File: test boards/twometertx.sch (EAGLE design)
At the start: 12 parts

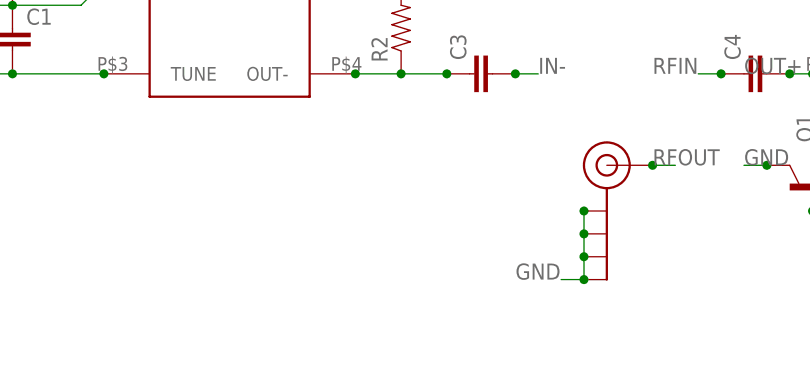
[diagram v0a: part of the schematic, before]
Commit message: 2 meter rx fixes
added ground pours and 4 pin header to the 2 meter rx for a test board.
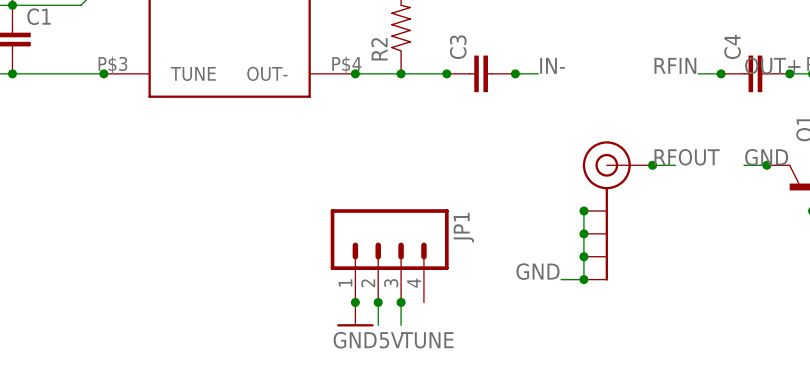
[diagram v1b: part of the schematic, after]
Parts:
- added JP1: (no value), SparkFun-Connectors:M04LONGPADS
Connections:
- net 5V: now also JP1.2
- net GND: now also JP1.1
- net TUNE: now also JP1.3
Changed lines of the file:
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@@
 <?xml version="1.0" encoding="utf-8"?>
 <!DOCTYPE eagle SYSTEM "eagle.dtd">
-<eagle version="7.2.0">
+<eagle version="7.3.0">
 <drawing>
 <settings>
@@
 <layer number="56" name="wert" color="7" fill="1" visible="no" active="no"/>
 <layer number="57" name="tCAD" color="7" fill="1" visible="no" active="no"/>
+<layer number="59" name="tCarbon" color="7" fill="1" visible="no" active="no"/>
+<layer number="60" name="bCarbon" color="7" fill="1" visible="no" active="no"/>
 <layer number="90" name="Modules" color="5" fill="1" visible="yes" active="yes"/>
 <layer number="91" name="Nets" color="2" fill="1" visible="yes" active="yes"/>
@@
 <layer number="113" name="IDFDebug" color="4" fill="1" visible="yes" active="yes"/>
 <layer number="116" name="Patch_BOT" color="9" fill="4" visible="yes" active="yes"/>
+<layer number="118" name="Rect_Pads" color="7" fill="1" visible="yes" active="yes"/>
 <layer number="121" name="_tsilk" color="7" fill="1" visible="yes" active="yes"/>
 <layer number="122" name="_bsilk" color="7" fill="1" visible="yes" active="yes"/>
@@
 <layer number="127" name="_tValues" color="7" fill="1" visible="yes" active="yes"/>
 <layer number="128" name="_bValues" color="7" fill="1" visible="yes" active="yes"/>
+<layer number="129" name="Mask" color="7" fill="1" visible="yes" active="yes"/>
 <layer number="131" name="tAdjust" color="7" fill="1" visible="yes" active="yes"/>
 <layer number="132" name="bAdjust" color="7" fill="1" visible="yes" active="yes"/>
@@
 <layer number="223" name="223bmp" color="24" fill="1" visible="no" active="no"/>
 <layer number="224" name="224bmp" color="25" fill="1" visible="no" active="no"/>
+<layer number="225" name="225bmp" color="7" fill="1" visible="yes" active="yes"/>
+<layer number="226" name="226bmp" color="7" fill="1" visible="yes" active="yes"/>
+<layer number="227" name="227bmp" color="7" fill="1" visible="yes" active="yes"/>
+<layer number="228" name="228bmp" color="7" fill="1" visible="yes" active="yes"/>
+<layer number="229" name="229bmp" color="7" fill="1" visible="yes" active="yes"/>
+<layer number="230" name="230bmp" color="7" fill="1" visible="yes" active="yes"/>
+<layer number="231" name="231bmp" color="7" fill="1" visible="yes" active="yes"/>
 <layer number="248" name="Housing" color="7" fill="1" visible="yes" active="yes"/>
 <layer number="249" name="Edge" color="7" fill="1" visible="yes" active="yes"/>
@@
 <layer number="251" name="SMDround" color="12" fill="11" visible="no" active="no"/>
 <layer number="254" name="cooling" color="7" fill="1" visible="yes" active="yes"/>
+<layer number="255" name="routoute" color="7" fill="1" visible="yes" active="yes"/>
 </layers>
 <schematic xreflabel="%F%N/%S.%C%R" xrefpart="/%S.%C%R">
@@
 <part name="J$1" library="SparkFun-Connectors" deviceset="SMA_EDGE" device=""/>
 <part name="Q1" library="SparkFun-DiscreteSemi" deviceset="TRANSISTOR_NPN" device="SOT89"/>
+<part name="JP1" library="SparkFun-Connectors" deviceset="M04" device="LONGPADS"/>
+<part name="GND2" library="SparkFun-Aesthetics" deviceset="GND" device=""/>
 </parts>
 <sheets>
@@
 <instance part="J$1" gate="1" x="86.36" y="30.48"/>
 <instance part="Q1" gate="G$1" x="109.22" y="27.94" rot="R90"/>
+<instance part="JP1" gate="G$1" x="60.96" y="20.32" rot="R270"/>
+<instance part="GND2" gate="1" x="58.42" y="12.7"/>
 </instances>
 <busses>
@@
 <label x="76.2" y="17.78" size="1.778" layer="95"/>
 </segment>
+<segment>
+<pinref part="JP1" gate="G$1" pin="1"/>
+<pinref part="GND2" gate="1" pin="GND"/>
+<junction x="58.42" y="15.24"/>
+</segment>
 </net>
 <net name="TUNE" class="0">
@@
 <junction x="30.48" y="40.64"/>
 <label x="10.16" y="40.64" size="1.778" layer="95"/>
+</segment>
+<segment>
+<wire x1="63.5" y1="15.24" x2="63.5" y2="12.7" width="0.1524" layer="91"/>
+<label x="63.5" y="10.16" size="1.778" layer="95"/>
+<pinref part="JP1" gate="G$1" pin="3"/>
+<junction x="63.5" y="15.24"/>
 </segment>
 </net>
@@
 <junction x="139.7" y="60.96"/>
 </segment>
-</net>
+<segment>
+<wire x1="60.96" y1="12.7" x2="60.96" y2="15.24" width="0.1524" layer="91"/>
+<label x="60.96" y="10.16" size="1.778" layer="95"/>
+<pinref part="JP1" gate="G$1" pin="2"/>
+<junction x="60.96" y="15.24"/>
+</segment>
+</net>

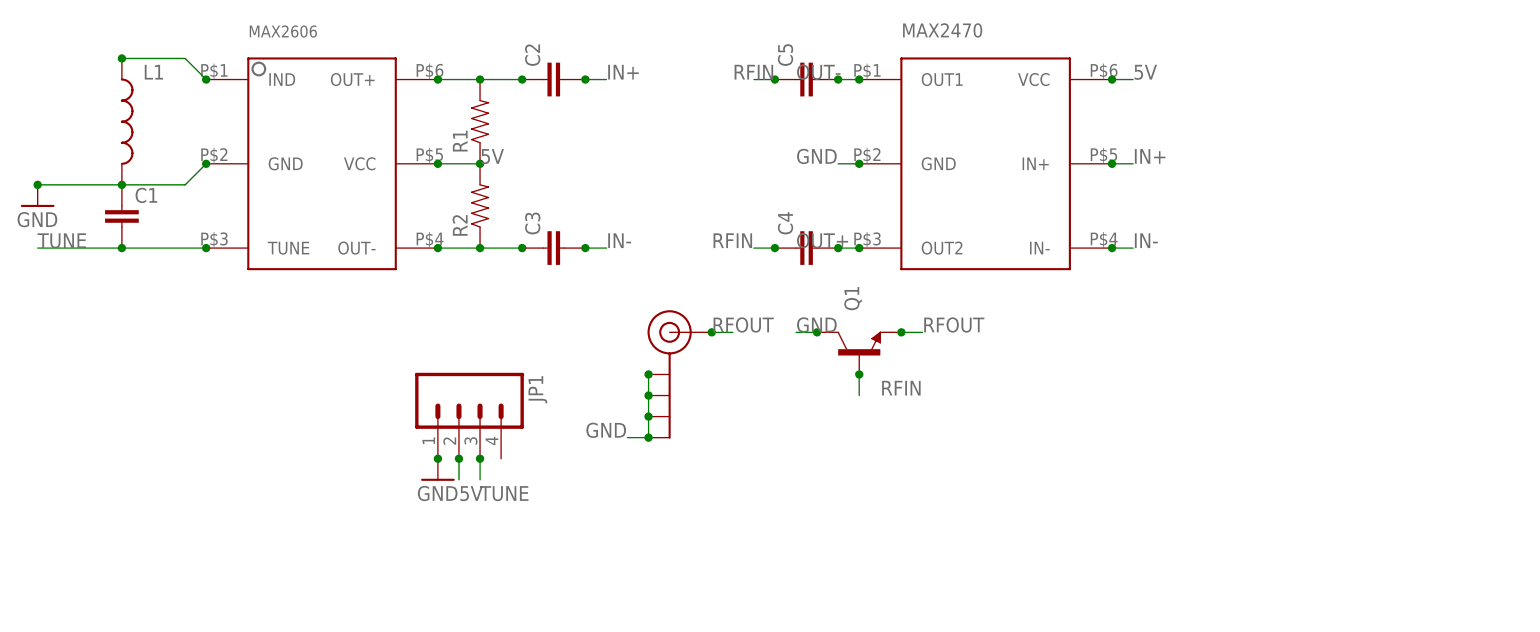
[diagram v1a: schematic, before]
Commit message: 2 meter tx rf amp bias
added bias circuit to RF amplifier
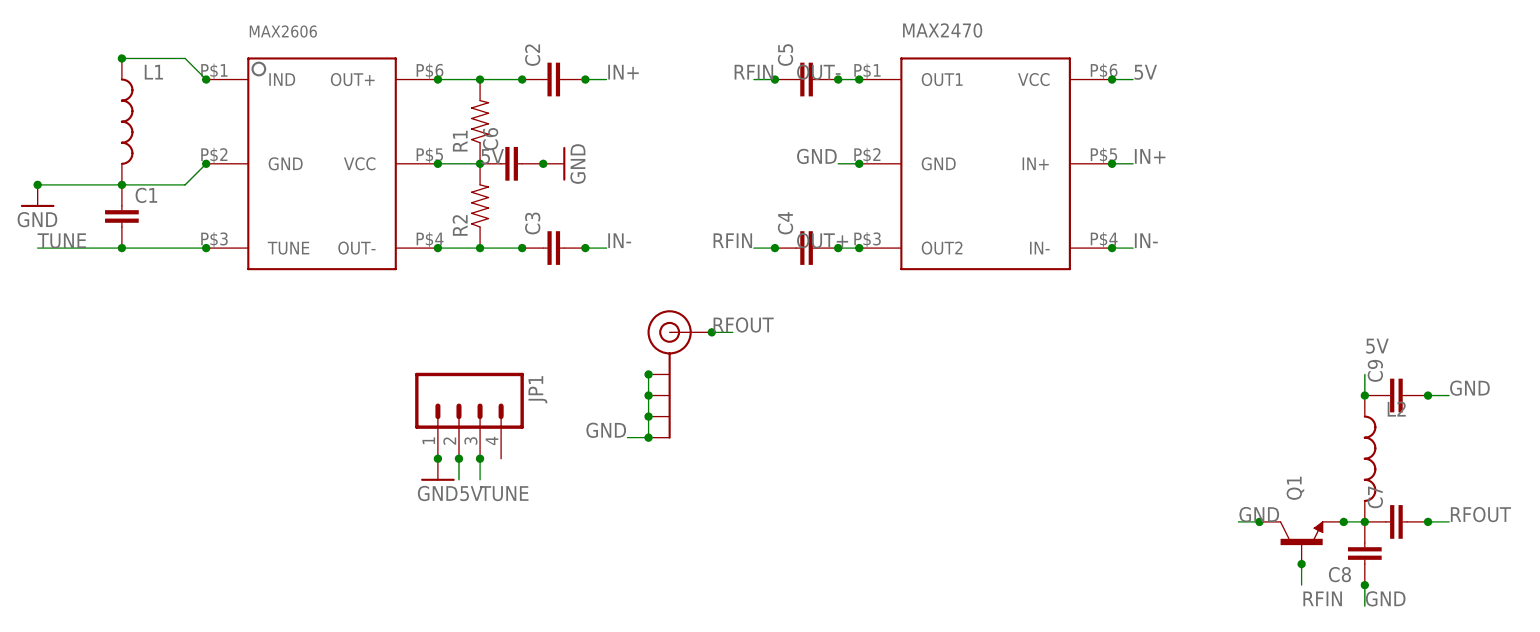
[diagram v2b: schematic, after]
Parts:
- added C6, C7, C8, C9: (no value), SparkFun-Capacitors:CAP0805
- added L2: (no value), SparkFun-Passives:INDUCTOR0805
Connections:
- new net N$3: C7.1, C8.2, L2.2, Q1.E
- net 5V: now also C6.1, C9.1, L2.1
- net GND: now also C6.2, C8.1, C9.2
- net RFOUT: now also C7.2; no longer Q1.E
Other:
- moved on the sheet: Q1
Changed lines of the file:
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@@
 <part name="JP1" library="SparkFun-Connectors" deviceset="M04" device="LONGPADS"/>
 <part name="GND2" library="SparkFun-Aesthetics" deviceset="GND" device=""/>
+<part name="C6" library="SparkFun-Capacitors" deviceset="CAP" device="0805"/>
+<part name="GND3" library="SparkFun-Aesthetics" deviceset="GND" device=""/>
+<part name="L2" library="SparkFun-Passives" deviceset="INDUCTOR" device="0805"/>
+<part name="C7" library="SparkFun-Capacitors" deviceset="CAP" device="0805"/>
+<part name="C8" library="SparkFun-Capacitors" deviceset="CAP" device="0805"/>
+<part name="C9" library="SparkFun-Capacitors" deviceset="CAP" device="0805"/>
 </parts>
 <sheets>
@@
 <instance part="C5" gate="G$1" x="104.14" y="60.96" rot="R90"/>
 <instance part="J$1" gate="1" x="86.36" y="30.48"/>
-<instance part="Q1" gate="G$1" x="109.22" y="27.94" rot="R90"/>
+<instance part="Q1" gate="G$1" x="162.56" y="5.08" rot="R90"/>
 <instance part="JP1" gate="G$1" x="60.96" y="20.32" rot="R270"/>
 <instance part="GND2" gate="1" x="58.42" y="12.7"/>
+<instance part="C6" gate="G$1" x="68.58" y="50.8" rot="R90"/>
+<instance part="GND3" gate="1" x="73.66" y="50.8" rot="R90"/>
+<instance part="L2" gate="G$1" x="170.18" y="15.24"/>
+<instance part="C7" gate="G$1" x="175.26" y="7.62" rot="R90"/>
+<instance part="C8" gate="G$1" x="170.18" y="5.08" rot="R180"/>
+<instance part="C9" gate="G$1" x="175.26" y="22.86" rot="R90"/>
 </instances>
 <busses>
@@
 <segment>
 <pinref part="Q1" gate="G$1" pin="C"/>
-<wire x1="104.14" y1="30.48" x2="101.6" y2="30.48" width="0.1524" layer="91"/>
-<junction x="104.14" y="30.48"/>
-<label x="101.6" y="30.48" size="1.778" layer="95"/>
+<wire x1="157.48" y1="7.62" x2="154.94" y2="7.62" width="0.1524" layer="91"/>
+<junction x="157.48" y="7.62"/>
+<label x="154.94" y="7.62" size="1.778" layer="95"/>
 </segment>
 <segment>
@@
 <junction x="58.42" y="15.24"/>
 </segment>
+<segment>
+<pinref part="C6" gate="G$1" pin="2"/>
+<pinref part="GND3" gate="1" pin="GND"/>
+<junction x="71.12" y="50.8"/>
+</segment>
+<segment>
+<pinref part="C9" gate="G$1" pin="2"/>
+<wire x1="177.8" y1="22.86" x2="180.34" y2="22.86" width="0.1524" layer="91"/>
+<label x="180.34" y="22.86" size="1.778" layer="95"/>
+<junction x="177.8" y="22.86"/>
+</segment>
+<segment>
+<pinref part="C8" gate="G$1" pin="1"/>
+<wire x1="170.18" y1="0" x2="170.18" y2="-2.54" width="0.1524" layer="91"/>
+<label x="170.18" y="-2.54" size="1.778" layer="95"/>
+<junction x="170.18" y="0"/>
+</segment>
 </net>
 <net name="TUNE" class="0">
@@
 <pinref part="R2" gate="G$1" pin="2"/>
 <junction x="63.5" y="50.8"/>
+<pinref part="C6" gate="G$1" pin="1"/>
 </segment>
 <segment>
@@
 <pinref part="JP1" gate="G$1" pin="2"/>
 <junction x="60.96" y="15.24"/>
+</segment>
+<segment>
+<pinref part="L2" gate="G$1" pin="1"/>
+<pinref part="C9" gate="G$1" pin="1"/>
+<wire x1="170.18" y1="22.86" x2="170.18" y2="25.4" width="0.1524" layer="91"/>
+<junction x="170.18" y="22.86"/>
+<label x="170.18" y="27.94" size="1.778" layer="95"/>
 </segment>
 </net>
@@
 <segment>
 <pinref part="Q1" gate="G$1" pin="B"/>
-<wire x1="109.22" y1="25.4" x2="109.22" y2="22.86" width="0.1524" layer="91"/>
-<junction x="109.22" y="25.4"/>
-<label x="111.76" y="22.86" size="1.778" layer="95"/>
+<wire x1="162.56" y1="2.54" x2="162.56" y2="0" width="0.1524" layer="91"/>
+<junction x="162.56" y="2.54"/>
+<label x="162.56" y="-2.54" size="1.778" layer="95"/>
 </segment>
 </net>
 <net name="RFOUT" class="0">
-<segment>
-<pinref part="Q1" gate="G$1" pin="E"/>
-<wire x1="114.3" y1="30.48" x2="116.84" y2="30.48" width="0.1524" layer="91"/>
-<junction x="114.3" y="30.48"/>
-<label x="116.84" y="30.48" size="1.778" layer="95"/>
-</segment>
 <segment>
 <pinref part="J$1" gate="1" pin="SIGNAL"/>
@@
 <label x="91.44" y="30.48" size="1.778" layer="95"/>
 </segment>
-</net>
+<segment>
+<pinref part="C7" gate="G$1" pin="2"/>
+<wire x1="177.8" y1="7.62" x2="180.34" y2="7.62" width="0.1524" layer="91"/>
+<label x="180.34" y="7.62" size="1.778" layer="95"/>
+<junction x="177.8" y="7.62"/>
+</segment>
+</net>
+<net name="N$3" class="0">
+<segment>
+<pinref part="L2" gate="G$1" pin="2"/>
+<pinref part="C7" gate="G$1" pin="1"/>
+<pinref part="C8" gate="G$1" pin="2"/>
+<junction x="170.18" y="7.62"/>
+<pinref part="C8" gate="G$1" pin="2"/>
+<pinref part="Q1" gate="G$1" pin="E"/>
+<wire x1="167.64" y1="7.62" x2="170.18" y2="7.62" width="0.1524" layer="91"/>
+<junction x="167.64" y="7.62"/>
+</segment>
+</net>
